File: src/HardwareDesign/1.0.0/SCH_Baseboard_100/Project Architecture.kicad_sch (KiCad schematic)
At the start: 0 parts

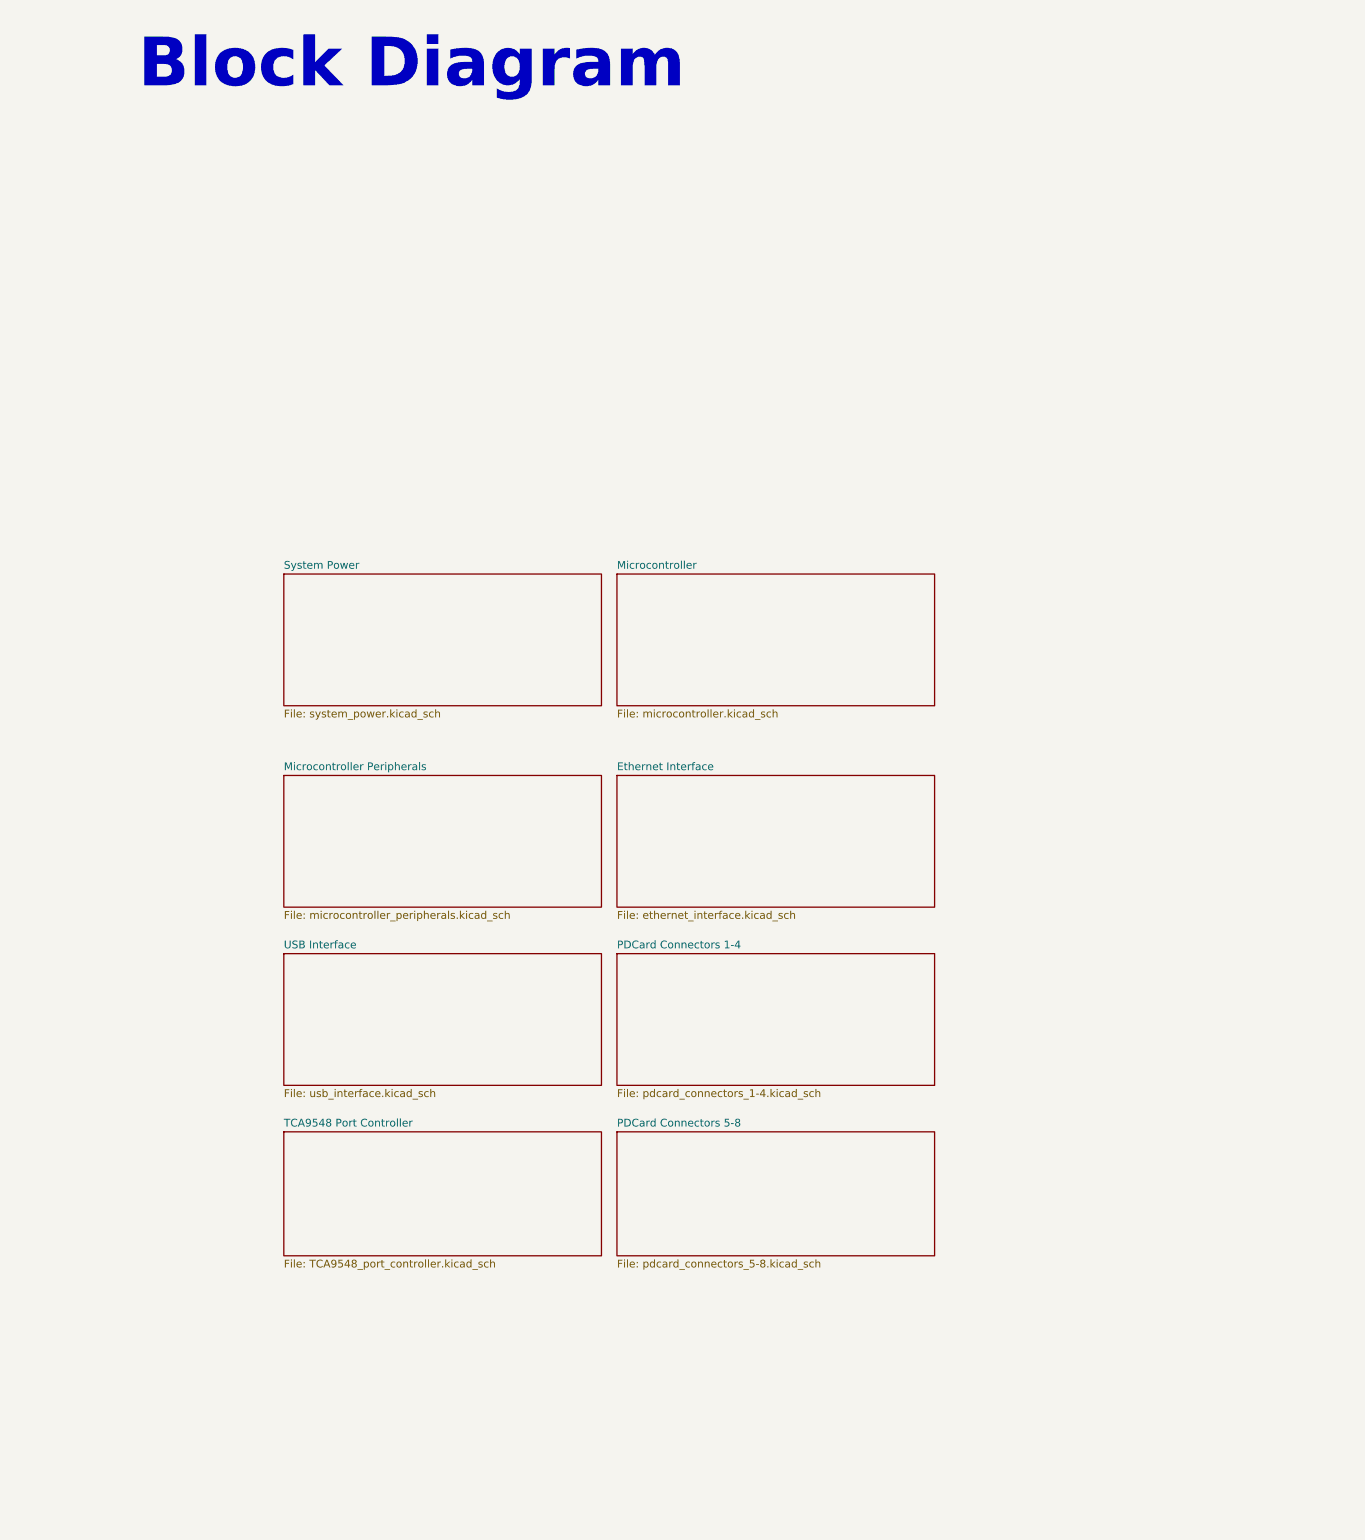
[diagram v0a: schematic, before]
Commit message: Add bladecore to design
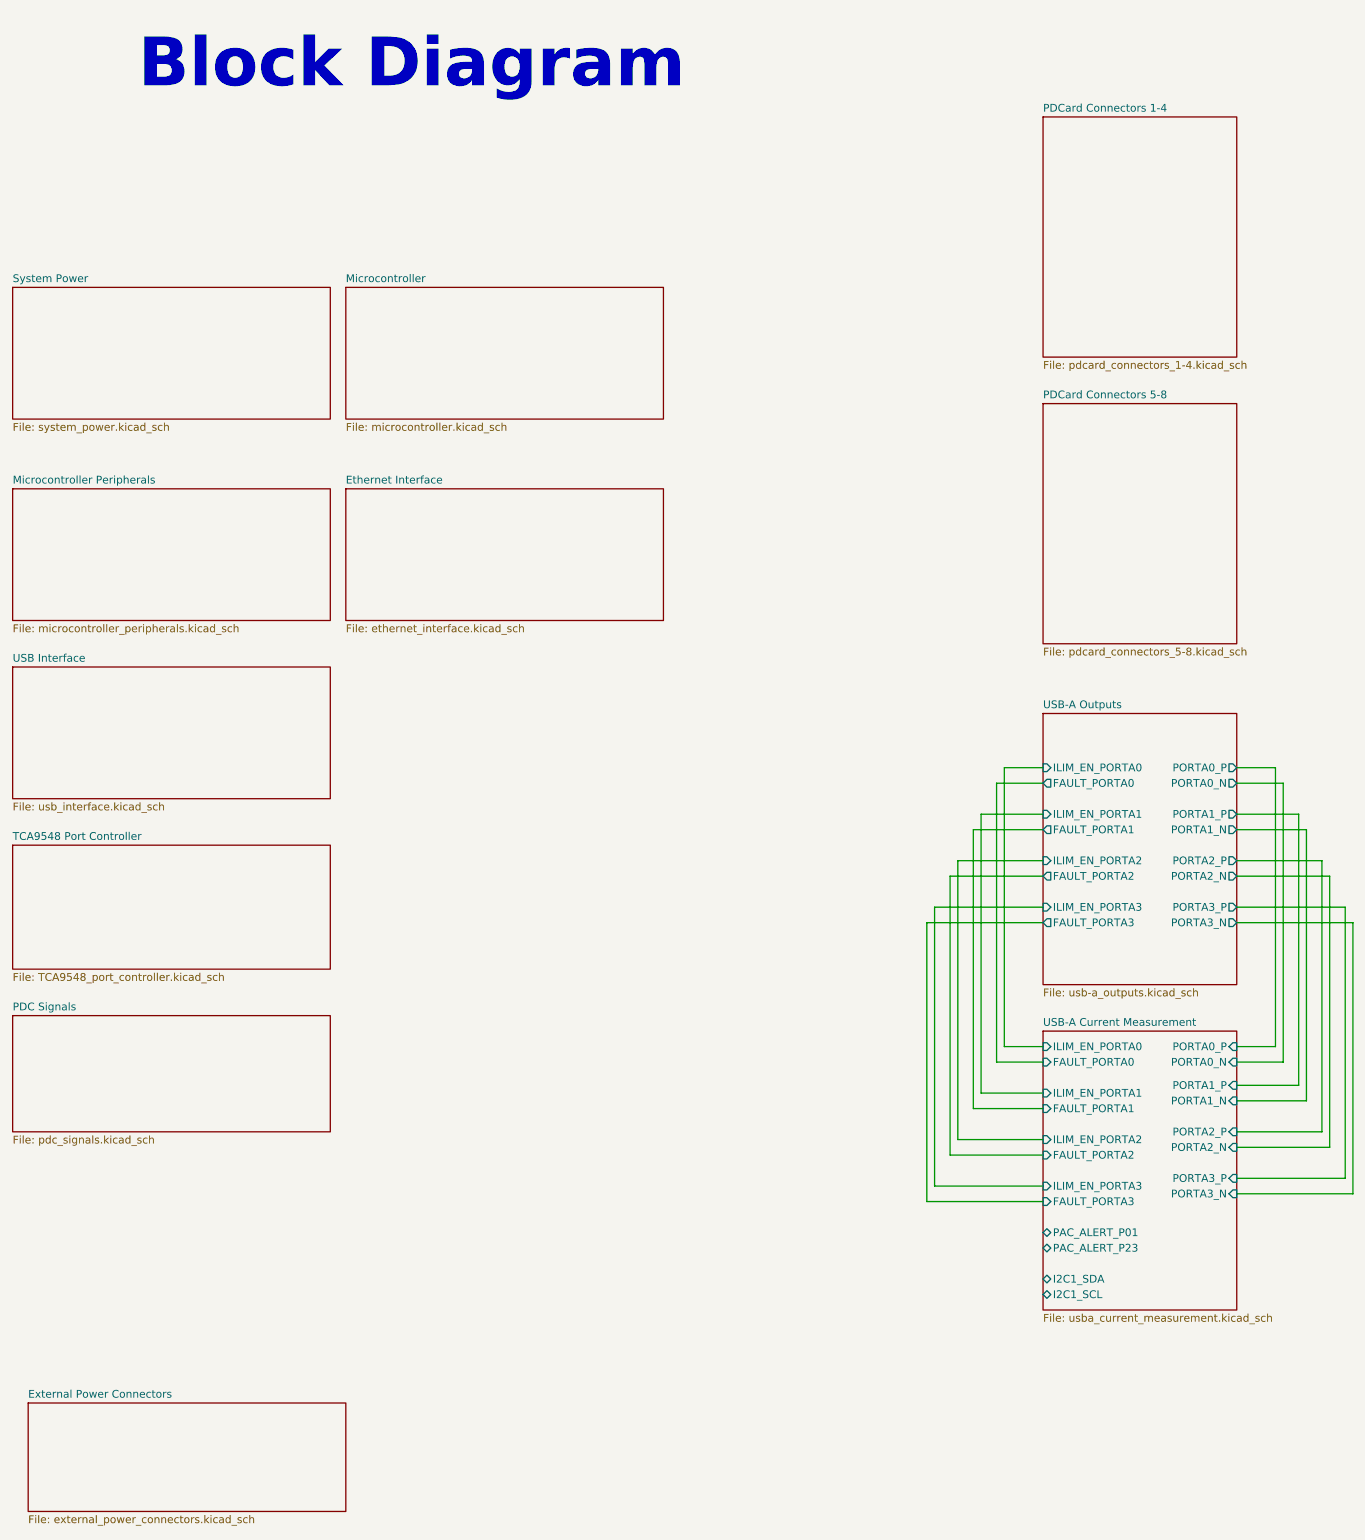
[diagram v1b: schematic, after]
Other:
- added sheet External Power Connectors (external_power_connectors.kicad_sch)
- added sheet PDC Signals (pdc_signals.kicad_sch)
- added sheet USB-A Current Measurement (usba_current_measurement.kicad_sch)
- added sheet USB-A Outputs (usb-a_outputs.kicad_sch)
